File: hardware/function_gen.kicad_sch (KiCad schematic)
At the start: 30 parts, among them J1 Conn_01x01, J10 Conn_01x01, J11 Conn_01x01, J12 Conn_01x01, J2 Conn_ARM_SWD_TagConnect_TC203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, J3 Conn_01x08, SW1 SW_SPDT, SW2 SW_Push, U1 STM32G431CBTx, Y1 Crystal_GND24

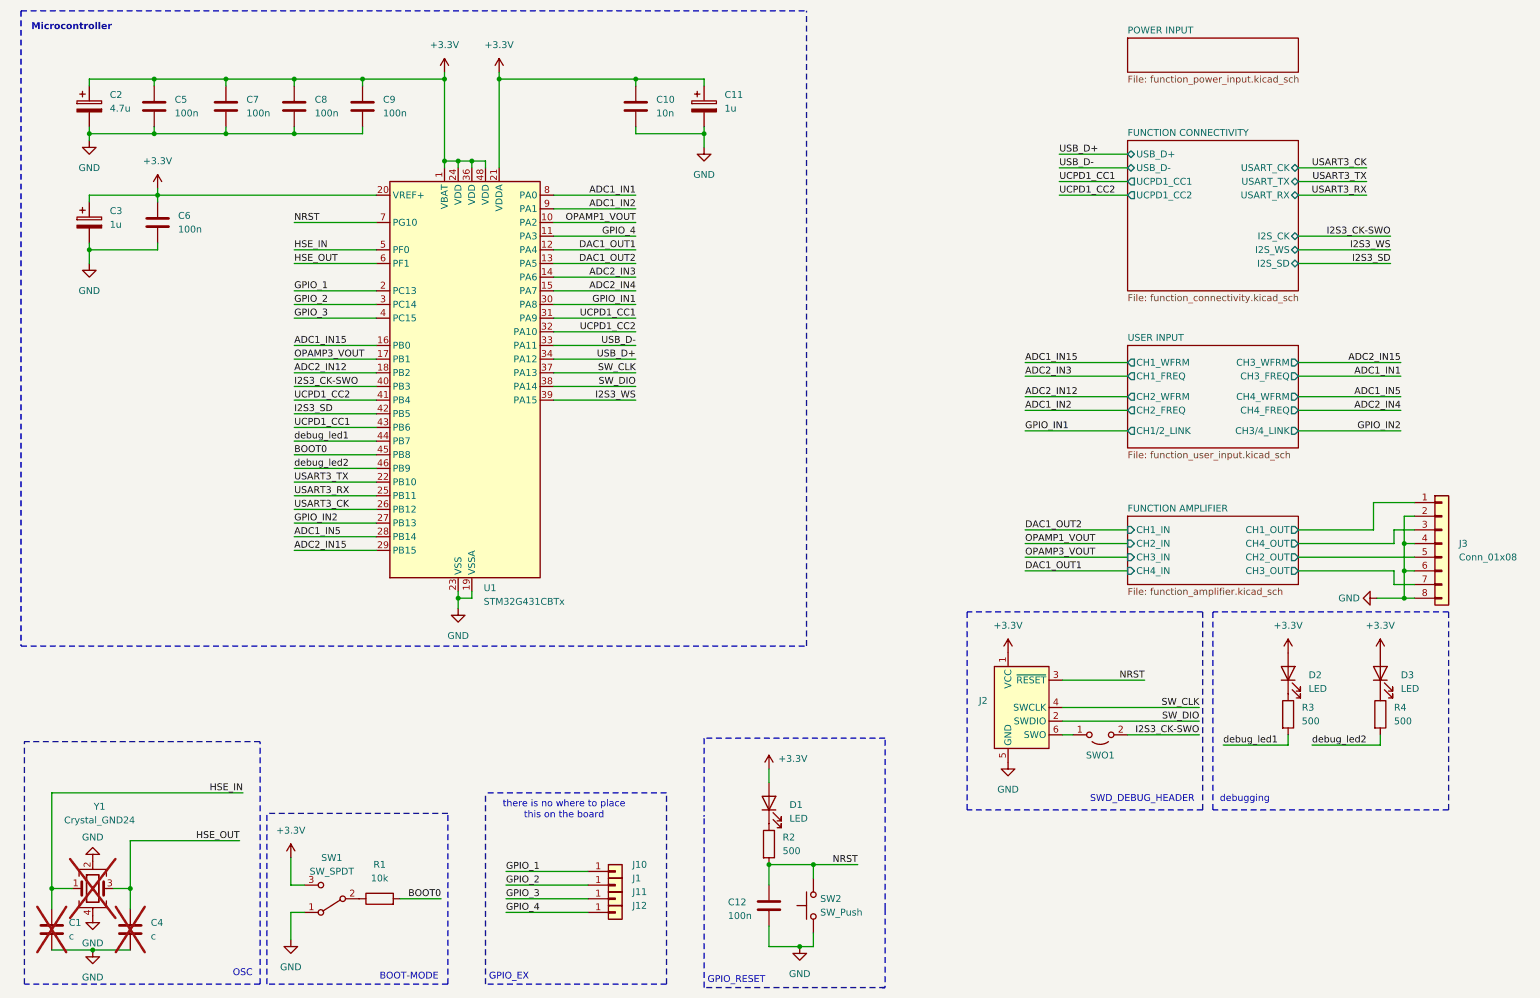
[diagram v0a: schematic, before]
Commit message: added RGB LEDs
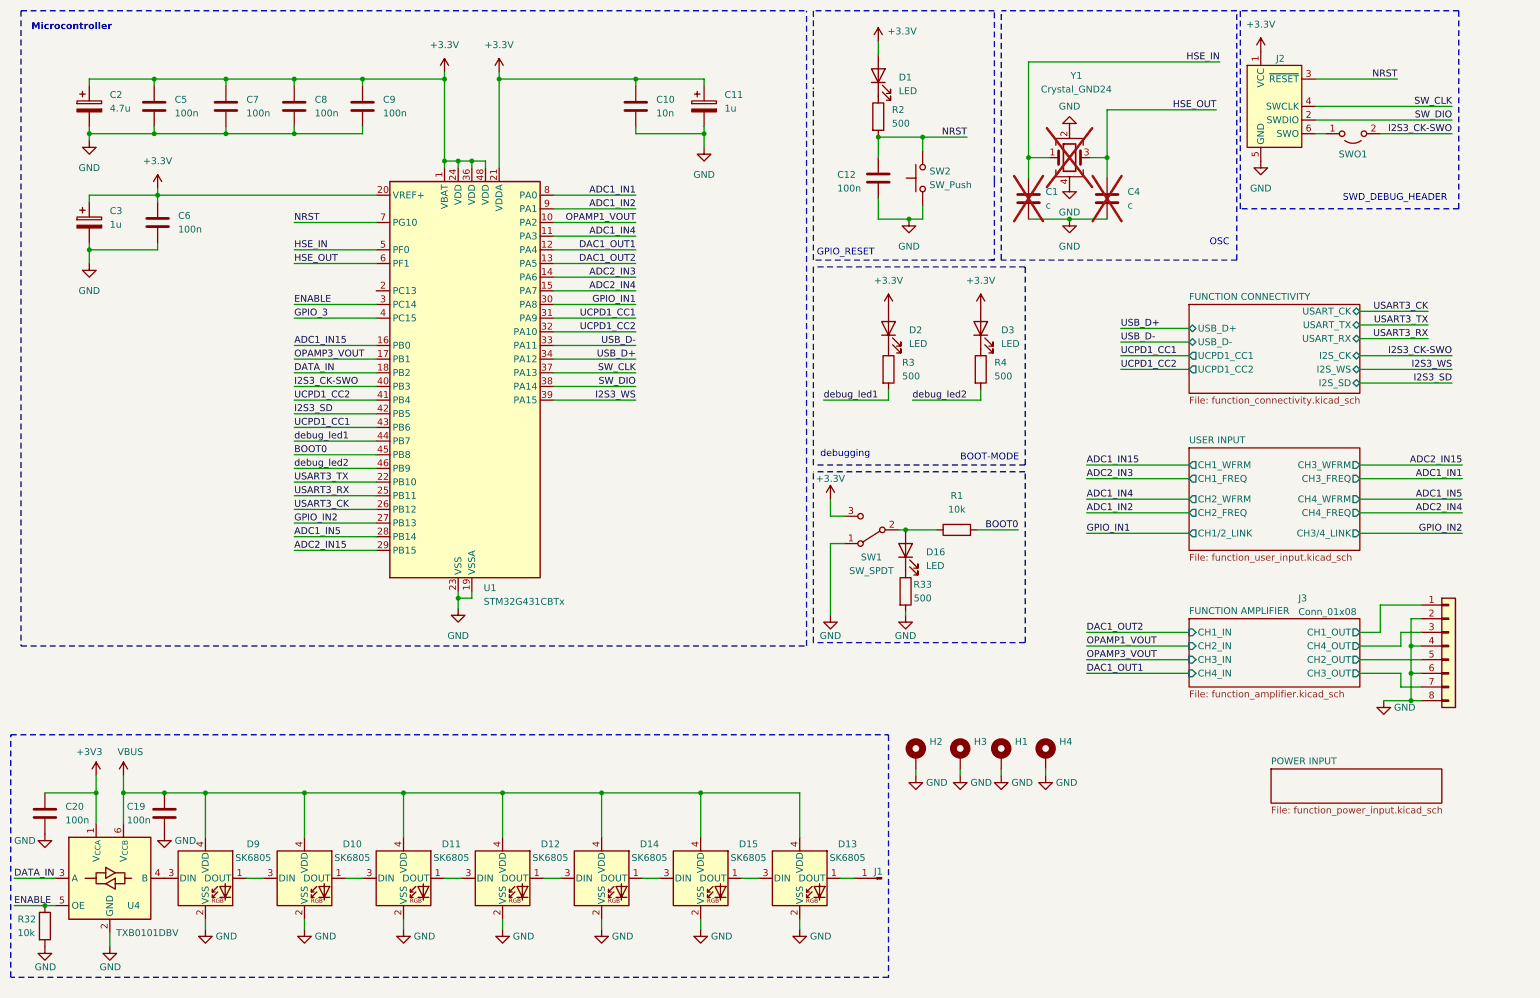
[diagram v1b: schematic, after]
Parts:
- removed J1, J10, J11, J12: Conn_01x01, TestPoint:TestPoint_Pad_1.0x1.0mm, symbol Connector_Generic:Conn_01x01
- added C19, C20: 100n, Capacitor_SMD:C_0805_2012Metric, symbol Device:C
- added D10, D11, D12, D13, D14, D15, D9: SK6805, LED_SMD:LED_SK6805_PLCC4_2.4x2.7mm_P1.3mm, symbol LED:SK6805
- added D16: LED, LED_SMD:LED_0805_2012Metric, symbol Device:LED
- added H1, H2, H3: MountingHole_Pad, MountingHole:MountingHole_3.2mm_M3_DIN965_Pad, symbol Mechanical:MountingHole_Pad
- added H4: MountingHole_Pad, MountingHole:MountingHole_3.2mm_M3_DIN965, symbol Mechanical:MountingHole_Pad
- added J1: Conn_01x01_Pin, symbol Connector:Conn_01x01_Pin
- added R32: 10k, Resistor_SMD:R_0805_2012Metric, symbol Device:R
- added R33: 500, Resistor_SMD:R_0805_2012Metric, symbol Device:R
- added U4: TXB0101DBV, Package_TO_SOT_SMD:SOT-23-6, symbol Logic_LevelTranslator:TXB0101DBV
- SW1: footprint Button_Switch_THT:SW_CuK_OS102011MA1QN1_SPDT_Angled -> Button_Switch_THT:SW_Slide_SPDT_Angled_CK_OS102011MA1Q
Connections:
- net GND: now also C19.2, C20.2, D10.2 (VSS), D11.2 (VSS), D12.2 (VSS), D13.2 (VSS), D14.2 (VSS), D15.2 (VSS), D9.2 (VSS), H1.1, H2.1, H3.1, H4.1, R32.2, R33.2, U4.2 (GND)
- net at R1.1, SW1.2 (B): now also D16.2 (A)
- net ADC2_IN12 renamed DATA_IN
- net DATA_IN: now also U4.3 (A)
- net GPIO_1: no longer names the net of U1.2 (PC13)
- net GPIO_2 renamed ENABLE
- net ENABLE: now also R32.1, U4.5 (OE)
- net GPIO_4 renamed ADC1_IN4
- new net: D13.1 (DOUT), J1.1 (Pin_1)
- new net: D13.3 (DIN), D15.1 (DOUT)
- new net: D16.1 (K), R33.1
- new net: D11.1 (DOUT), D12.3 (DIN)
- new net: D10.1 (DOUT), D11.3 (DIN)
- new net: D10.3 (DIN), D9.1 (DOUT)
- new net: D9.3 (DIN), U4.4 (B)
- new net: D14.1 (DOUT), D15.3 (DIN)
- new net: D12.1 (DOUT), D14.3 (DIN)
- new net +3V3: C20.1, U4.1 (V_{CCA})
- new net VBUS: C19.1, D10.4 (VDD), D11.4 (VDD), D12.4 (VDD), D13.4 (VDD), D14.4 (VDD), D15.4 (VDD), D9.4 (VDD), U4.6 (V_{CCB})
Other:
- note removed: "GPIO_EX"
- note removed: "there is no where to place this on the board"
- moved on the sheet: C1, C12, C4, D1, D2, D3, J2, J3, R1, R2, R3, R4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

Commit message: updated
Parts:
- removed H1, H2, H3: MountingHole_Pad, MountingHole:MountingHole_3.2mm_M3_DIN965_Pad, symbol Mechanical:MountingHole_Pad
- removed H4: MountingHole_Pad, MountingHole:MountingHole_3.2mm_M3_DIN965, symbol Mechanical:MountingHole_Pad
- J1: footprint (none) -> TestPoint:TestPoint_Pad_1.5x1.5mm
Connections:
- net +3V3 is gone; now on net +3.3V: C20.1, U4.1 (V_{CCA})
- net FUNCTION AMPLIFIER/CH1_OUT: now also J3.3 (Pin_3); no longer J3.1 (Pin_1)
- net FUNCTION AMPLIFIER/CH3_OUT: now also J3.1 (Pin_1); no longer J3.7 (Pin_7)
- net FUNCTION AMPLIFIER/CH4_OUT: now also J3.7 (Pin_7); no longer J3.3 (Pin_3)
